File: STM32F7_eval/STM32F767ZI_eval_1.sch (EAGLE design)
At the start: 89 parts, among them CN1 GROVE-4P-CONN-I2C-90D, CN2 GROVE-4P-CONN-I2C-90D, CN3 GROVE-4P-CONN-I2C-90D, CN4 GROVE-4P-CONN-AN01-90D, CN5 ARDUINO_COMPAT_IF, CN6 STLINKV21_SWD_IF, CN7 WFT0750CZ09-SMD_, CN8 MCO_IF, CN9 UART_IF, Q1 PMF370XN_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

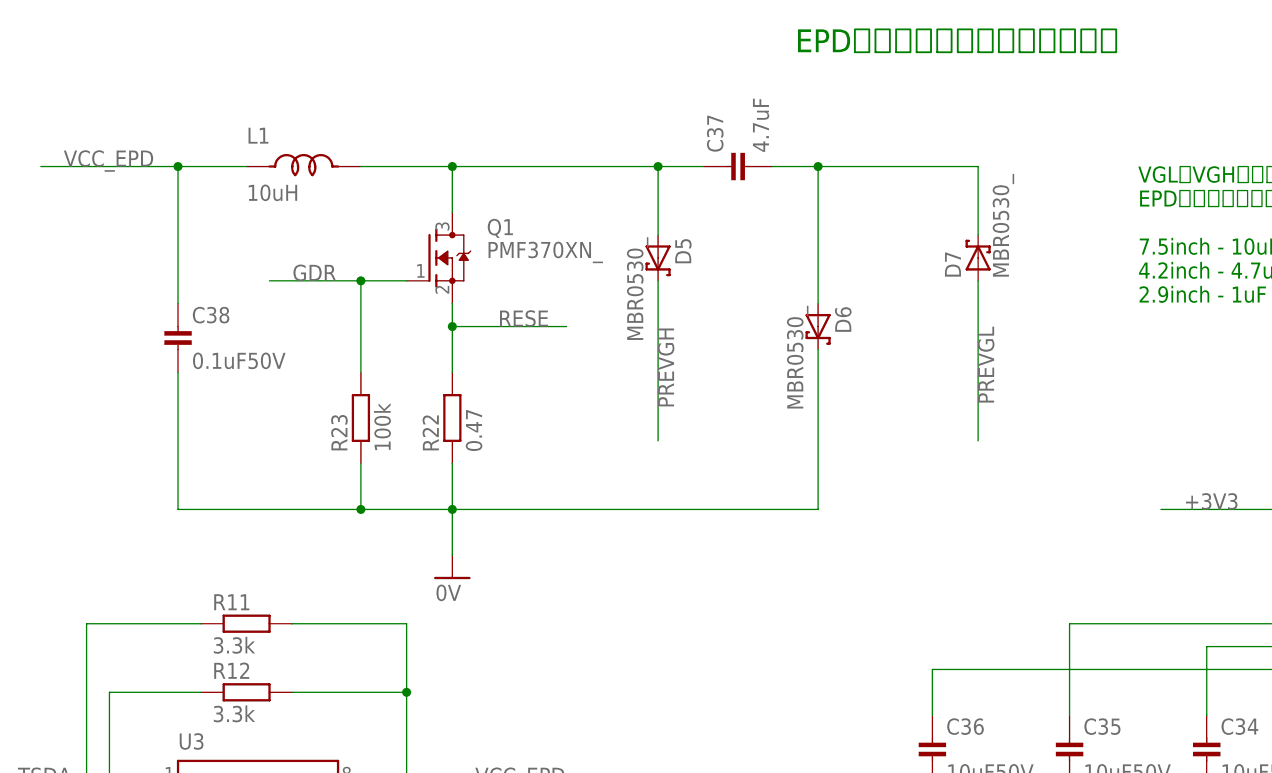
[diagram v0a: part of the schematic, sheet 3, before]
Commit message: 評価基板を修正
・手はんだ用パターンに修正
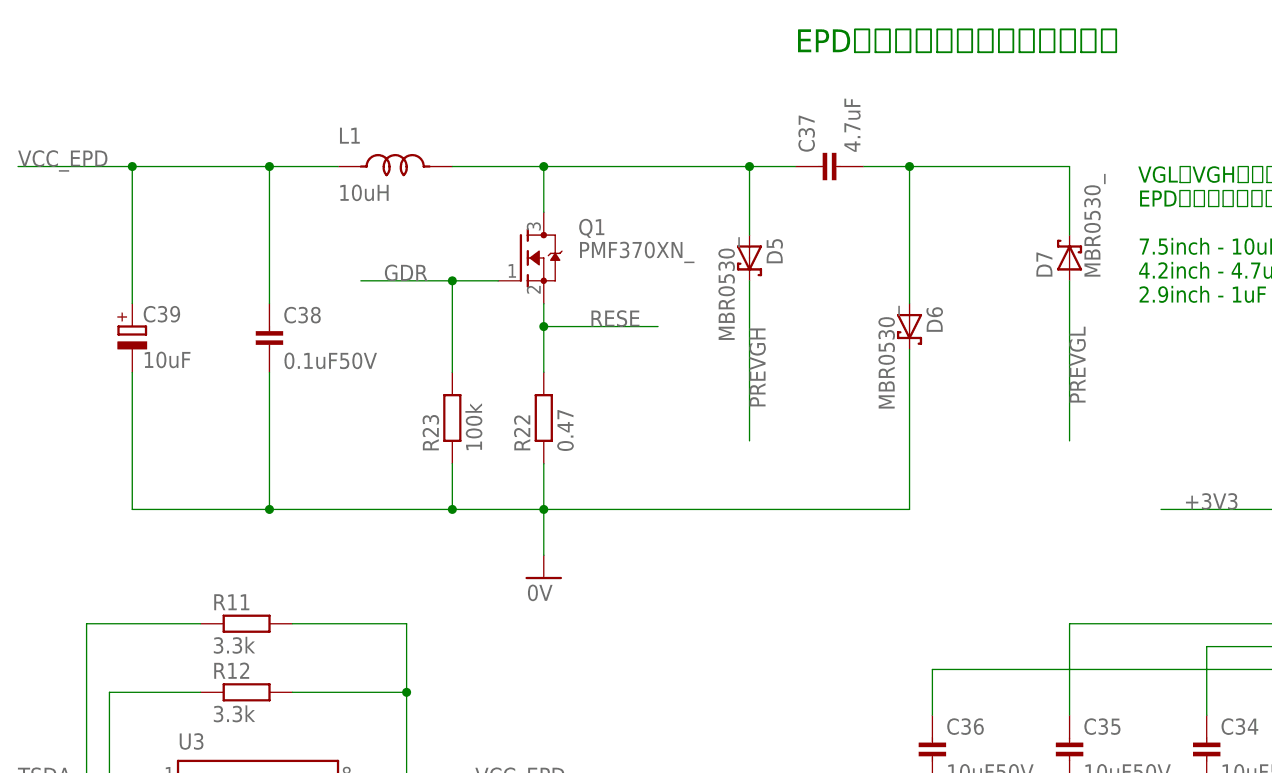
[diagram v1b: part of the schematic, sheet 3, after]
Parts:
- added C39: 10uF, Parts:TPST106K016R0800_
- C38: device Parts:CAP_0805_DEV -> Parts:CAP_0603_DEV
- R11, R12: device Parts:RESISTOR_0603_DEV -> Parts:RESISTOR_0805_DEV
- SW1, SW2: value SKRPACE010 -> SKRPACE010_; device Parts:SKRPACE010 -> Parts:SKRPACE010_
- U1: value STM32F767ZI -> STM32F767ZI_; device Parts:STM32F767ZI -> Parts:STM32F767ZI_
- U2: value LD39050PU33R -> LD39050PU33R_DEV; device Parts:LD39050PU33R -> Parts:LD39050PU33R_DEV
- U4: value TSV631AICT -> TSV631AICT_; device Parts:TSV631AICT -> Parts:TSV631AICT_
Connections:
- net 0V: now also C39.-
- net VCC_EPD: now also C39.+
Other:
- moved on the sheet: C24, C37, C38, D5, D6, D7, L1, Q1, R22, R23

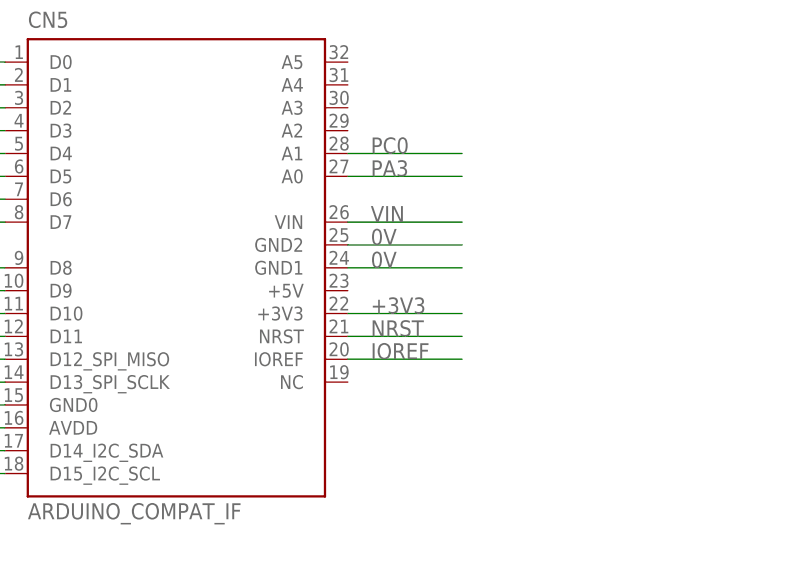
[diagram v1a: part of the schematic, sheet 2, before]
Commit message: 評価基板を修正
・シルクの位置などを調整
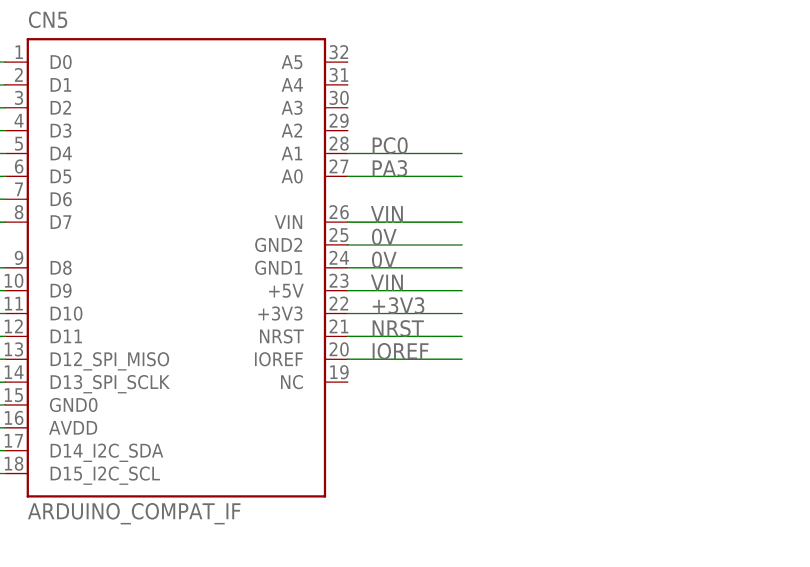
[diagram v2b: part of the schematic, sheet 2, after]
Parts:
- C22: device Parts:CAP_0603_DEV -> Parts:CAP_0805_DEV
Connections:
- net VIN: now also CN5.+5V
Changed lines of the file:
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@@
 <setting verticaltext="up"/>
 </settings>
-<grid distance="0.1" unitdist="inch" unit="inch" style="lines" multiple="1" display="yes" altdistance="0.01" altunitdist="inch" altunit="inch"/>
+<grid distance="0.1" unitdist="inch" unit="inch" style="lines" multiple="1" display="no" altdistance="0.01" altunitdist="inch" altunit="inch"/>
 <layers>
 <layer number="1" name="Top" color="4" fill="1" visible="no" active="no"/>
@@
 <layer number="91" name="Nets" color="2" fill="1" visible="yes" active="yes"/>
 <layer number="92" name="Busses" color="1" fill="1" visible="yes" active="yes"/>
-<layer number="93" name="Pins" color="2" fill="1" visible="yes" active="yes"/>
+<layer number="93" name="Pins" color="2" fill="1" visible="no" active="yes"/>
 <layer number="94" name="Symbols" color="4" fill="1" visible="yes" active="yes"/>
 <layer number="95" name="Names" color="7" fill="1" visible="yes" active="yes"/>
@@
 <part name="C24" library="Parts" deviceset="TPST*" device="106K016R0800_" value="10uF"/>
 <part name="R10" library="Parts" deviceset="RESISTOR" device="_0603_DEV" value="0"/>
-<part name="C22" library="Parts" deviceset="CAP" device="_0603_DEV" value="4.7uF"/>
+<part name="C22" library="Parts" deviceset="CAP" device="_0805_DEV" value="4.7uF"/>
 <part name="GND9" library="Supply" deviceset="0V" device=""/>
 <part name="FB1" library="Parts" deviceset="BLM21PG" device="300SN1D"/>
@@
 <label x="20.32" y="55.88" size="1.778" layer="95"/>
 </segment>
-</net>
+<segment>
+<pinref part="CN5" gate="G$1" pin="+5V"/>
+<wire x1="129.54" y1="132.08" x2="142.24" y2="132.08" width="0.1524" layer="91"/>
+<label x="132.08" y="132.08" size="1.778" layer="95"/>
+</segment>
+</net>

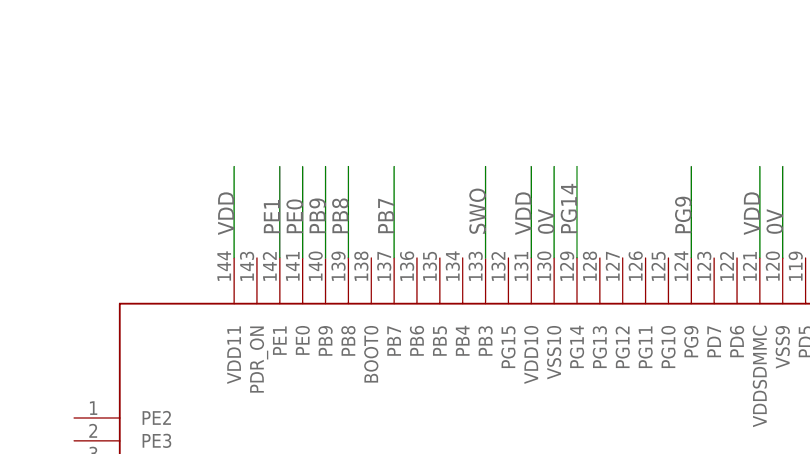
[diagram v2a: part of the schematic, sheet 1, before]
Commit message: 評価基板を修正
・バイパスコンデンサー修正
・配線欠落箇所を修正
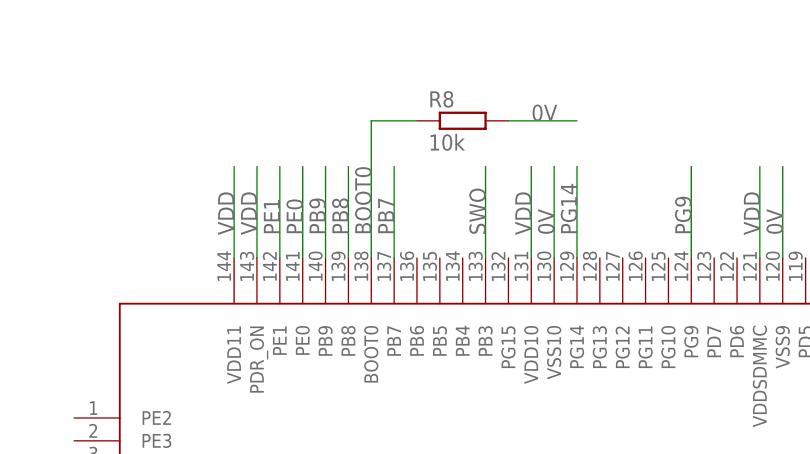
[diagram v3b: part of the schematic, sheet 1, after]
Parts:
- added R8: 10k, Parts:RESISTOR_0603_DEV
- C20, C21: device Parts:CAP_0603_DEV -> Parts:CAP_1206
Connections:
- new net BOOT0: R8.1, U1.BOOT0
- net 0V: now also R8.2
- net VDD: now also U1.PDR_ON
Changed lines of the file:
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@@
 <setting verticaltext="up"/>
 </settings>
-<grid distance="0.1" unitdist="inch" unit="inch" style="lines" multiple="1" display="no" altdistance="0.01" altunitdist="inch" altunit="inch"/>
+<grid distance="0.1" unitdist="inch" unit="inch" style="lines" multiple="1" display="yes" altdistance="0.01" altunitdist="inch" altunit="inch"/>
 <layers>
-<layer number="1" name="Top" color="4" fill="1" visible="no" active="no"/>
-<layer number="2" name="Route2" color="1" fill="3" visible="no" active="no"/>
-<layer number="3" name="Route3" color="4" fill="3" visible="no" active="no"/>
-<layer number="14" name="Route14" color="1" fill="6" visible="no" active="no"/>
-<layer number="15" name="Route15" color="4" fill="6" visible="no" active="no"/>
-<layer number="16" name="Bottom" color="1" fill="1" visible="no" active="no"/>
-<layer number="17" name="Pads" color="2" fill="1" visible="no" active="no"/>
-<layer number="18" name="Vias" color="2" fill="1" visible="no" active="no"/>
-<layer number="19" name="Unrouted" color="6" fill="1" visible="no" active="no"/>
-<layer number="20" name="Dimension" color="15" fill="1" visible="no" active="no"/>
-<layer number="21" name="tPlace" color="7" fill="1" visible="no" active="no"/>
-<layer number="22" name="bPlace" color="7" fill="1" visible="no" active="no"/>
-<layer number="23" name="tOrigins" color="15" fill="1" visible="no" active="no"/>
-<layer number="24" name="bOrigins" color="15" fill="1" visible="no" active="no"/>
-<layer number="25" name="tNames" color="7" fill="1" visible="no" active="no"/>
-<layer number="26" name="bNames" color="7" fill="1" visible="no" active="no"/>
-<layer number="27" name="tValues" color="7" fill="1" visible="no" active="no"/>
-<layer number="28" name="bValues" color="7" fill="1" visible="no" active="no"/>
+<layer number="1" name="Top" color="4" fill="1" visible="yes" active="no"/>
+<layer number="2" name="Route2" color="1" fill="3" visible="yes" active="no"/>
+<layer number="3" name="Route3" color="4" fill="3" visible="yes" active="no"/>
+<layer number="14" name="Route14" color="1" fill="6" visible="yes" active="no"/>
+<layer number="15" name="Route15" color="4" fill="6" visible="yes" active="no"/>
+<layer number="16" name="Bottom" color="1" fill="1" visible="yes" active="no"/>
+<layer number="17" name="Pads" color="2" fill="1" visible="yes" active="no"/>
+<layer number="18" name="Vias" color="2" fill="1" visible="yes" active="no"/>
+<layer number="19" name="Unrouted" color="6" fill="1" visible="yes" active="no"/>
+<layer number="20" name="Dimension" color="15" fill="1" visible="yes" active="no"/>
+<layer number="21" name="tPlace" color="7" fill="1" visible="yes" active="no"/>
+<layer number="22" name="bPlace" color="7" fill="1" visible="yes" active="no"/>
+<layer number="23" name="tOrigins" color="15" fill="1" visible="yes" active="no"/>
+<layer number="24" name="bOrigins" color="15" fill="1" visible="yes" active="no"/>
+<layer number="25" name="tNames" color="7" fill="1" visible="yes" active="no"/>
+<layer number="26" name="bNames" color="7" fill="1" visible="yes" active="no"/>
+<layer number="27" name="tValues" color="7" fill="1" visible="yes" active="no"/>
+<layer number="28" name="bValues" color="7" fill="1" visible="yes" active="no"/>
 <layer number="29" name="tStop" color="7" fill="3" visible="no" active="no"/>
 <layer number="30" name="bStop" color="7" fill="6" visible="no" active="no"/>
@@
 <layer number="35" name="tGlue" color="7" fill="4" visible="no" active="no"/>
 <layer number="36" name="bGlue" color="7" fill="5" visible="no" active="no"/>
-<layer number="37" name="tTest" color="7" fill="1" visible="no" active="no"/>
-<layer number="38" name="bTest" color="7" fill="1" visible="no" active="no"/>
+<layer number="37" name="tTest" color="7" fill="1" visible="yes" active="no"/>
+<layer number="38" name="bTest" color="7" fill="1" visible="yes" active="no"/>
 <layer number="39" name="tKeepout" color="4" fill="11" visible="no" active="no"/>
 <layer number="40" name="bKeepout" color="1" fill="11" visible="no" active="no"/>
@@
 <layer number="44" name="Drills" color="7" fill="1" visible="no" active="no"/>
 <layer number="45" name="Holes" color="7" fill="1" visible="no" active="no"/>
-<layer number="46" name="Milling" color="3" fill="1" visible="no" active="no"/>
-<layer number="47" name="Measures" color="7" fill="1" visible="no" active="no"/>
-<layer number="48" name="Document" color="7" fill="1" visible="no" active="no"/>
-<layer number="49" name="Reference" color="7" fill="1" visible="no" active="no"/>
-<layer number="50" name="dxf" color="7" fill="1" visible="no" active="no"/>
-<layer number="51" name="tDocu" color="7" fill="1" visible="no" active="no"/>
-<layer number="52" name="bDocu" color="7" fill="1" visible="no" active="no"/>
-<layer number="53" name="tGND_GNDA" color="7" fill="9" visible="no" active="no"/>
-<layer number="54" name="bGND_GNDA" color="1" fill="9" visible="no" active="no"/>
-<layer number="56" name="wert" color="7" fill="1" visible="no" active="no"/>
-<layer number="57" name="tCAD" color="7" fill="1" visible="no" active="no"/>
-<layer number="59" name="tCarbon" color="7" fill="1" visible="no" active="no"/>
-<layer number="60" name="bCarbon" color="7" fill="1" visible="no" active="no"/>
+<layer number="46" name="Milling" color="3" fill="1" visible="yes" active="no"/>
+<layer number="47" name="Measures" color="7" fill="1" visible="yes" active="no"/>
+<layer number="48" name="Document" color="7" fill="1" visible="yes" active="no"/>
+<layer number="49" name="Reference" color="7" fill="1" visible="yes" active="no"/>
+<layer number="50" name="dxf" color="7" fill="1" visible="yes" active="no"/>
+<layer number="51" name="tDocu" color="7" fill="1" visible="yes" active="no"/>
+<layer number="52" name="bDocu" color="7" fill="1" visible="yes" active="no"/>
+<layer number="53" name="tGND_GNDA" color="7" fill="9" visible="yes" active="no"/>
+<layer number="54" name="bGND_GNDA" color="1" fill="9" visible="yes" active="no"/>
+<layer number="56" name="wert" color="7" fill="1" visible="yes" active="no"/>
+<layer number="57" name="tCAD" color="7" fill="1" visible="yes" active="no"/>
+<layer number="59" name="tCarbon" color="7" fill="1" visible="yes" active="no"/>
+<layer number="60" name="bCarbon" color="7" fill="1" visible="yes" active="no"/>
 <layer number="90" name="Modules" color="5" fill="1" visible="yes" active="yes"/>
 <layer number="91" name="Nets" color="2" fill="1" visible="yes" active="yes"/>
@@
 <part name="R9" library="Parts" deviceset="RESISTOR" device="_0603_DEV" value="0"/>
 <part name="GND6" library="Supply" deviceset="0V" device=""/>
-<part name="C20" library="Parts" deviceset="CAP" device="_0603_DEV" value="2.2uF X7R"/>
-<part name="C21" library="Parts" deviceset="CAP" device="_0603_DEV" value="2.2uF X7R"/>
+<part name="C20" library="Parts" deviceset="CAP" device="_1206" value="2.2uF X7R"/>
+<part name="C21" library="Parts" deviceset="CAP" device="_1206" value="2.2uF X7R"/>
 <part name="GND7" library="Supply" deviceset="0V" device=""/>
 <part name="U2" library="Parts" deviceset="LD39050PU33R" device="_DEV" value="LD39050PU33R_DEV"/>
@@
 <part name="CN9" library="PartsForProto" deviceset="UART_IF" device=""/>
 <part name="C39" library="Parts" deviceset="TPST*" device="106K016R0800_" value="10uF"/>
+<part name="R8" library="Parts" deviceset="RESISTOR" device="_0603_DEV" value="10k"/>
 </parts>
 <sheets>
@@
 <instance part="+3V2" gate="G$1" x="20.32" y="200.66"/>
 <instance part="+3V3" gate="G$1" x="83.82" y="241.3"/>
+<instance part="R8" gate="G$1" x="167.64" y="233.68"/>
 </instances>
 <busses>
@@
 <junction x="320.04" y="187.96"/>
 </segment>
+<segment>
+<pinref part="R8" gate="G$1" pin="2"/>
+<wire x1="177.8" y1="233.68" x2="185.42" y2="233.68" width="0.1524" layer="91"/>
+<label x="180.34" y="233.68" size="1.778" layer="95"/>
+</segment>
 </net>
 <net name="N$2" class="0">
@@
 <label x="17.78" y="99.06" size="1.778" layer="95" rot="R90"/>
 </segment>
+<segment>
+<pinref part="U1" gate="G$1" pin="PDR_ON"/>
+<wire x1="149.86" y1="218.44" x2="149.86" y2="228.6" width="0.1524" layer="91"/>
+<label x="149.86" y="220.98" size="1.778" layer="95" rot="R90"/>
+</segment>
 </net>
 <net name="PD9" class="0">
@@
 </segment>
 </net>
+<net name="BOOT0" class="0">
+<segment>
+<pinref part="U1" gate="G$1" pin="BOOT0"/>
+<wire x1="162.56" y1="218.44" x2="162.56" y2="233.68" width="0.1524" layer="91"/>
+<pinref part="R8" gate="G$1" pin="1"/>
+<wire x1="162.56" y1="233.68" x2="167.64" y2="233.68" width="0.1524" layer="91"/>
+<label x="162.56" y="220.98" size="1.778" layer="95" rot="R90"/>
+</segment>
+</net>
